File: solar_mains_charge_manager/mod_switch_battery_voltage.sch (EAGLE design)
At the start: 31 parts, among them IC1 ACS750LCA-050, T1 TIP122, X10 22-23-2041, X2 22-23-2021, X3 22-23-2031, X5 22-23-2031, X6 22-23-2041, X7 53047-15, X8 53047-15

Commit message: A lot of stuff
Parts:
- removed D1, D2, D3, D4, D8: 1N4004, diode:1N4004
- removed D5, D7: (no value), diode:ZENER-DIODEDO34-7
- removed IC1: ACS750LCA-050, allegro:ACS750LCA-050
- removed OK2: PC817, optocoupler:PC817
- removed R10, R12, R5, R9: (no value), resistor:R-EU_0204/5
- removed R6, R7: (no value), resistor:R-EU_0204/7
- removed U$1: NANO, Arduino-clone:NANO
- removed X10, X6: 22-23-2041, con-molex:22-23-2041
- removed X3, X5: 22-23-2031, con-molex:22-23-2031
- removed X7, X8: 53047-15, con-molex:53047-15
- added X1: 22-23-2051, con-molex:22-23-2051
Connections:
- removed net N$1: U$1.3.3V, U$1.AREF, X7-13.S, X7-14.S
- removed net N$11: D1.C, D2.C, R7.2
- removed net N$12: OK2.COL, U$1.D12, X8-1.S
- removed net N$13: D1.A, D3.C
- removed net N$15: D2.A, D4.C, R6.1
- removed net N$16: R6.2
- removed net N$17: U$1.D11, X3-2.S, X8-2.S
- removed net N$18: U$1.D10, X3-3.S, X8-3.S
- removed net N$19: U$1.D9, X6-3.S, X8-4.S
- removed net N$2: R3.2, U$1.D13, X7-15.S
- removed net N$20: U$1.D8, X6-4.S, X8-5.S
- removed net N$21: U$1.RST, X6-2.S, X7-3.S
- removed net N$22: U$1.D7, X8-6.S
- removed net N$23: U$1.D6, X8-7.S
- removed net N$24: U$1.D5, X8-8.S
- removed net N$25: U$1.D4, X8-9.S
- removed net N$26: U$1.D3, X8-10.S
- removed net N$27: U$1.D2, X8-11.S
- removed net N$28: U$1.GND2, X8-12.S
- removed net N$29: U$1.RST1, X8-13.S
- removed net N$3: R10.2, R12.1, R9.2
- removed net N$30: U$1.RX1, X8-14.S
- removed net N$31: U$1.TX0, X8-15.S
- removed net N$32: U$1.5.5V, X7-4.S
- removed net N$33: U$1.A7, X7-5.S
- removed net N$34: U$1.A6, X7-6.S
- removed net N$35: U$1.A5, X7-7.S
- removed net N$36: U$1.A4, X7-8.S
- removed net N$37: U$1.A3, X7-9.S
- removed net N$38: U$1.A2, X7-10.S
- removed net N$39: D7.C, D8.C, R12.2, U$1.A1, X7-11.S
- removed net N$41: R10.1, X10-4.S
- removed net N$42: R9.1, X10-3.S
- removed net N$8: D3.A, D4.A, D5.A, OK2.C, R5.1
- removed net N$9: D5.C, OK2.A, R5.2, R7.1
- net 12V: now also X1-4.S; no longer U$1.RAW, X5-3.S, X7-1.S
- net BAT: now also X1-3.S; no longer X10-2.S, X5-2.S
- net GND: now also R4.1, X1-5.S; no longer D7.A, D8.A, OK2.EMIT, U$1.GND, X10-1.S, X3-1.S, X5-1.S, X6-1.S, X7-2.S
- net N$40: now also X1-1.S; no longer U$1.A0, X7-12.S
- net N$6: now also R3.2, X1-2.S; no longer OK1.EMIT, R4.1
- net N$7: now also OK1.EMIT
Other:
- moved on the sheet: D6, OK1, R1, R11, R2, R3, R4, T1, X2-1, X2-2

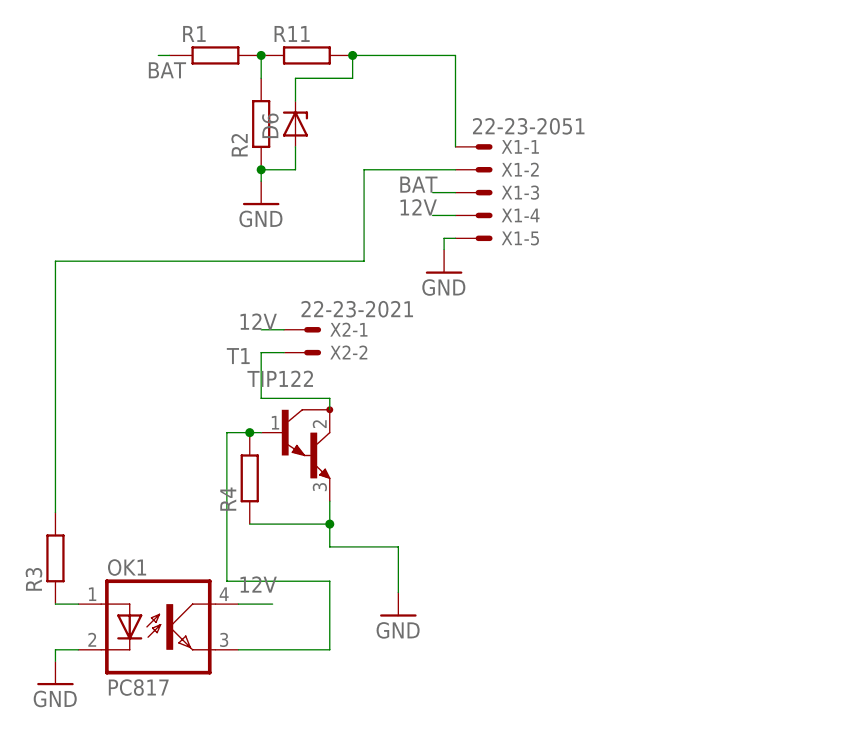
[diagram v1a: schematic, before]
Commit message: Finished board layout of mod_switch_battery_voltage and more work on psu_considerations.ods
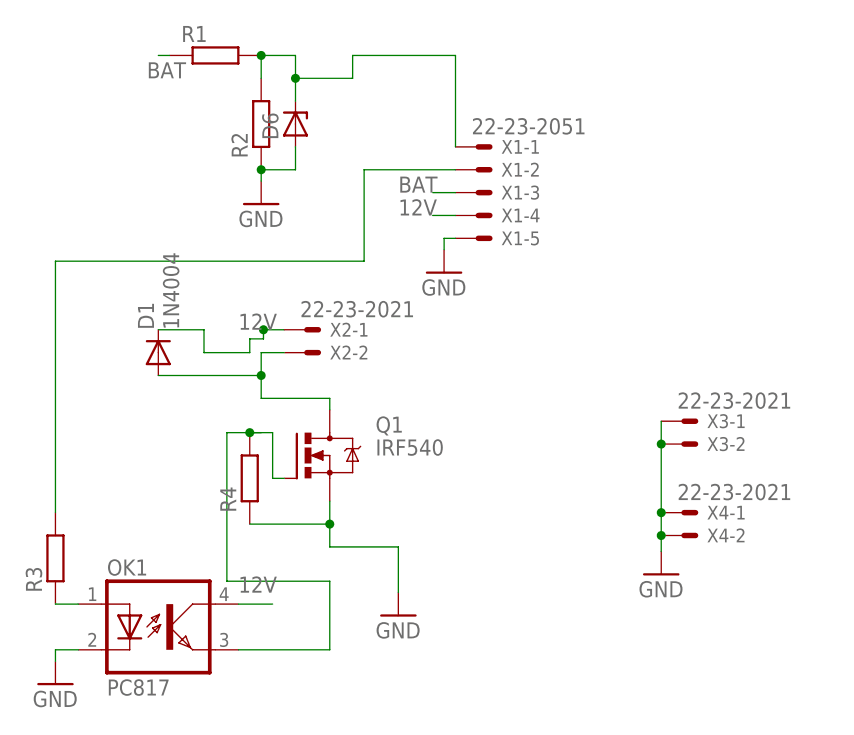
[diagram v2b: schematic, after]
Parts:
- removed R11: (no value), resistor:R-EU_0204/5
- removed T1: TIP122, transistor:TIP122
- added D1: 1N4004, diode:1N4004
- added Q1: IRF540, transistor-power:IRF540
- added X3, X4: 22-23-2021, con-molex:22-23-2021
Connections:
- removed net N$40: D6.C, R11.2, X1-1.S
- net 12V: now also D1.C
- net GND: now also Q1.S, X3-1.S, X3-2.S, X4-1.S, X4-2.S; no longer T1.E
- net N$43: now also D6.C, X1-1.S; no longer R11.1
- net N$5: now also D1.A, Q1.D; no longer T1.C
- net N$7: now also Q1.G; no longer T1.B
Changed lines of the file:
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@@
 <part name="GND7" library="supply1" library_urn="urn:adsk.eagle:library:371" deviceset="GND" device=""/>
 <part name="R4" library="resistor" library_urn="urn:adsk.eagle:library:348" deviceset="R-EU_" device="0204/5" package3d_urn="urn:adsk.eagle:package:25955/1"/>
-<part name="T1" library="transistor" library_urn="urn:adsk.eagle:library:402" deviceset="TIP122" device="" package3d_urn="urn:adsk.eagle:package:29897/1"/>
 <part name="R1" library="resistor" library_urn="urn:adsk.eagle:library:348" deviceset="R-EU_" device="0204/5" package3d_urn="urn:adsk.eagle:package:25955/1"/>
 <part name="R2" library="resistor" library_urn="urn:adsk.eagle:library:348" deviceset="R-EU_" device="0204/5" package3d_urn="urn:adsk.eagle:package:25955/1"/>
 <part name="GND1" library="supply1" library_urn="urn:adsk.eagle:library:371" deviceset="GND" device=""/>
 <part name="D6" library="diode" library_urn="urn:adsk.eagle:library:210" deviceset="ZENER-DIODE" device="DO34-7" package3d_urn="urn:adsk.eagle:package:43364/1"/>
-<part name="R11" library="resistor" library_urn="urn:adsk.eagle:library:348" deviceset="R-EU_" device="0204/5" package3d_urn="urn:adsk.eagle:package:25955/1"/>
 <part name="X1" library="con-molex" library_urn="urn:adsk.eagle:library:165" deviceset="22-23-2051" device=""/>
 <part name="GND2" library="supply1" library_urn="urn:adsk.eagle:library:371" deviceset="GND" device=""/>
+<part name="Q1" library="transistor-power" library_urn="urn:adsk.eagle:library:400" deviceset="IRF540" device="" package3d_urn="urn:adsk.eagle:package:29484/3"/>
+<part name="X3" library="con-molex" library_urn="urn:adsk.eagle:library:165" deviceset="22-23-2021" device=""/>
+<part name="X4" library="con-molex" library_urn="urn:adsk.eagle:library:165" deviceset="22-23-2021" device=""/>
+<part name="GND4" library="supply1" library_urn="urn:adsk.eagle:library:371" deviceset="GND" device=""/>
+<part name="D1" library="diode" library_urn="urn:adsk.eagle:library:210" deviceset="1N4004" device="" package3d_urn="urn:adsk.eagle:package:43336/1"/>
 </parts>
 <sheets>
@@
 <instance part="GND7" gate="1" x="115.57" y="8.89"/>
 <instance part="R4" gate="G$1" x="99.06" y="24.13" rot="R90"/>
-<instance part="T1" gate="G$1" x="102.87" y="29.21"/>
 <instance part="R1" gate="G$1" x="95.25" y="71.12"/>
 <instance part="R2" gate="G$1" x="100.33" y="63.5" rot="R90"/>
 <instance part="GND1" gate="1" x="100.33" y="54.61"/>
 <instance part="D6" gate="G$1" x="104.14" y="63.5" rot="R90"/>
-<instance part="R11" gate="G$1" x="105.41" y="71.12"/>
 <instance part="X1" gate="-1" x="124.46" y="60.96"/>
 <instance part="X1" gate="-2" x="124.46" y="58.42"/>
@@
 <instance part="X1" gate="-5" x="124.46" y="50.8"/>
 <instance part="GND2" gate="1" x="120.65" y="46.99"/>
+<instance part="Q1" gate="G$1" x="105.41" y="26.67"/>
+<instance part="X3" gate="-1" x="147.32" y="30.48"/>
+<instance part="X3" gate="-2" x="147.32" y="27.94"/>
+<instance part="X4" gate="-1" x="147.32" y="20.32"/>
+<instance part="X4" gate="-2" x="147.32" y="17.78"/>
+<instance part="GND4" gate="1" x="144.78" y="13.462"/>
+<instance part="D1" gate="1" x="88.9" y="38.1" rot="R90"/>
 </instances>
 <busses>
@@
 <wire x1="115.57" y1="16.51" x2="115.57" y2="11.43" width="0.1524" layer="91"/>
 <pinref part="GND7" gate="1" pin="GND"/>
-<pinref part="T1" gate="G$1" pin="E"/>
 <pinref part="R4" gate="G$1" pin="1"/>
 <wire x1="99.06" y1="19.05" x2="107.95" y2="19.05" width="0.1524" layer="91"/>
 <junction x="107.95" y="19.05"/>
+<pinref part="Q1" gate="G$1" pin="S"/>
 </segment>
 <segment>
@@
 <wire x1="120.65" y1="50.8" x2="120.65" y2="49.53" width="0.1524" layer="91"/>
 </segment>
+<segment>
+<pinref part="X3" gate="-1" pin="S"/>
+<pinref part="X3" gate="-2" pin="S"/>
+<wire x1="144.78" y1="30.48" x2="144.78" y2="27.94" width="0.1524" layer="91"/>
+<pinref part="X4" gate="-1" pin="S"/>
+<wire x1="144.78" y1="27.94" x2="144.78" y2="20.32" width="0.1524" layer="91"/>
+<junction x="144.78" y="27.94"/>
+<pinref part="X4" gate="-2" pin="S"/>
+<wire x1="144.78" y1="20.32" x2="144.78" y2="17.78" width="0.1524" layer="91"/>
+<junction x="144.78" y="20.32"/>
+<pinref part="GND4" gate="1" pin="GND"/>
+<wire x1="144.78" y1="17.78" x2="144.78" y2="16.002" width="0.1524" layer="91"/>
+<junction x="144.78" y="17.78"/>
+</segment>
 </net>
 <net name="N$4" class="0">
@@
 <segment>
 <pinref part="X2" gate="-1" pin="S"/>
-<wire x1="102.87" y1="40.64" x2="100.33" y2="40.64" width="0.1524" layer="91"/>
+<wire x1="102.87" y1="40.64" x2="100.584" y2="40.64" width="0.1524" layer="91"/>
 <label x="97.79" y="40.64" size="1.778" layer="95"/>
+<pinref part="D1" gate="1" pin="C"/>
+<wire x1="100.584" y1="40.64" x2="100.33" y2="40.64" width="0.1524" layer="91"/>
+<wire x1="88.9" y1="40.64" x2="93.98" y2="40.64" width="0.1524" layer="91"/>
+<wire x1="93.98" y1="40.64" x2="93.98" y2="38.1" width="0.1524" layer="91"/>
+<wire x1="93.98" y1="38.1" x2="99.06" y2="38.1" width="0.1524" layer="91"/>
+<wire x1="99.06" y1="38.1" x2="99.06" y2="39.624" width="0.1524" layer="91"/>
+<wire x1="99.06" y1="39.624" x2="100.584" y2="39.624" width="0.1524" layer="91"/>
+<wire x1="100.584" y1="39.624" x2="100.584" y2="40.64" width="0.1524" layer="91"/>
+<junction x="100.584" y="40.64"/>
 </segment>
 <segment>
@@
 <pinref part="X2" gate="-2" pin="S"/>
 <wire x1="102.87" y1="38.1" x2="100.33" y2="38.1" width="0.1524" layer="91"/>
-<pinref part="T1" gate="G$1" pin="C"/>
 <wire x1="107.95" y1="31.75" x2="107.95" y2="33.02" width="0.1524" layer="91"/>
 <wire x1="107.95" y1="33.02" x2="100.33" y2="33.02" width="0.1524" layer="91"/>
-<wire x1="100.33" y1="33.02" x2="100.33" y2="38.1" width="0.1524" layer="91"/>
+<wire x1="100.33" y1="33.02" x2="100.33" y2="35.56" width="0.1524" layer="91"/>
+<pinref part="Q1" gate="G$1" pin="D"/>
+<pinref part="D1" gate="1" pin="A"/>
+<wire x1="100.33" y1="35.56" x2="100.33" y2="38.1" width="0.1524" layer="91"/>
+<wire x1="88.9" y1="35.56" x2="100.33" y2="35.56" width="0.1524" layer="91"/>
+<junction x="100.33" y="35.56"/>
 </segment>
 </net>
@@
 <pinref part="R4" gate="G$1" pin="2"/>
 <wire x1="96.52" y1="29.21" x2="99.06" y2="29.21" width="0.1524" layer="91"/>
-<pinref part="T1" gate="G$1" pin="B"/>
 <wire x1="99.06" y1="29.21" x2="100.33" y2="29.21" width="0.1524" layer="91"/>
 <junction x="99.06" y="29.21"/>
+<wire x1="99.06" y1="29.21" x2="101.6" y2="29.21" width="0.1524" layer="91"/>
+<pinref part="Q1" gate="G$1" pin="G"/>
+<wire x1="101.6" y1="29.21" x2="101.6" y2="24.13" width="0.1524" layer="91"/>
+<wire x1="101.6" y1="24.13" x2="102.87" y2="24.13" width="0.1524" layer="91"/>
 </segment>
 </net>
@@
 </segment>
 </net>
-<net name="N$40" class="0">
-<segment>
-<pinref part="D6" gate="G$1" pin="C"/>
-<wire x1="104.14" y1="68.58" x2="104.14" y2="66.04" width="0.1524" layer="91"/>
-<pinref part="R11" gate="G$1" pin="2"/>
-<wire x1="104.14" y1="68.58" x2="110.49" y2="68.58" width="0.1524" layer="91"/>
-<wire x1="110.49" y1="68.58" x2="110.49" y2="71.12" width="0.1524" layer="91"/>
-<wire x1="110.49" y1="71.12" x2="121.92" y2="71.12" width="0.1524" layer="91"/>
-<junction x="110.49" y="71.12"/>
-<pinref part="X1" gate="-1" pin="S"/>
-<wire x1="121.92" y1="60.96" x2="121.92" y2="71.12" width="0.1524" layer="91"/>
-</segment>
-</net>
 <net name="N$43" class="0">
 <segment>
@@
 <pinref part="R1" gate="G$1" pin="2"/>
 <wire x1="100.33" y1="71.12" x2="100.33" y2="68.58" width="0.1524" layer="91"/>
-<pinref part="R11" gate="G$1" pin="1"/>
+<wire x1="100.33" y1="71.12" x2="104.14" y2="71.12" width="0.1524" layer="91"/>
 <junction x="100.33" y="71.12"/>
+<pinref part="D6" gate="G$1" pin="C"/>
+<wire x1="104.14" y1="68.58" x2="104.14" y2="66.04" width="0.1524" layer="91"/>
+<wire x1="104.14" y1="68.58" x2="110.49" y2="68.58" width="0.1524" layer="91"/>
+<wire x1="110.49" y1="68.58" x2="110.49" y2="71.12" width="0.1524" layer="91"/>
+<wire x1="110.49" y1="71.12" x2="121.92" y2="71.12" width="0.1524" layer="91"/>
+<pinref part="X1" gate="-1" pin="S"/>
+<wire x1="121.92" y1="60.96" x2="121.92" y2="71.12" width="0.1524" layer="91"/>
+<wire x1="104.14" y1="71.12" x2="104.14" y2="68.58" width="0.1524" layer="91"/>
+<junction x="104.14" y="68.58"/>
 </segment>
 </net>
